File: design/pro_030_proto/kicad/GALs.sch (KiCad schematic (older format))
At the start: 17 parts, among them IC10 ATF22V10C, IC2 ATF22V10C, IC3 ATF22V10C, IC4 ATF22V10C, IC5 ATF22V10C, IC6 ATF22V10C, IC7 ATF22V10C

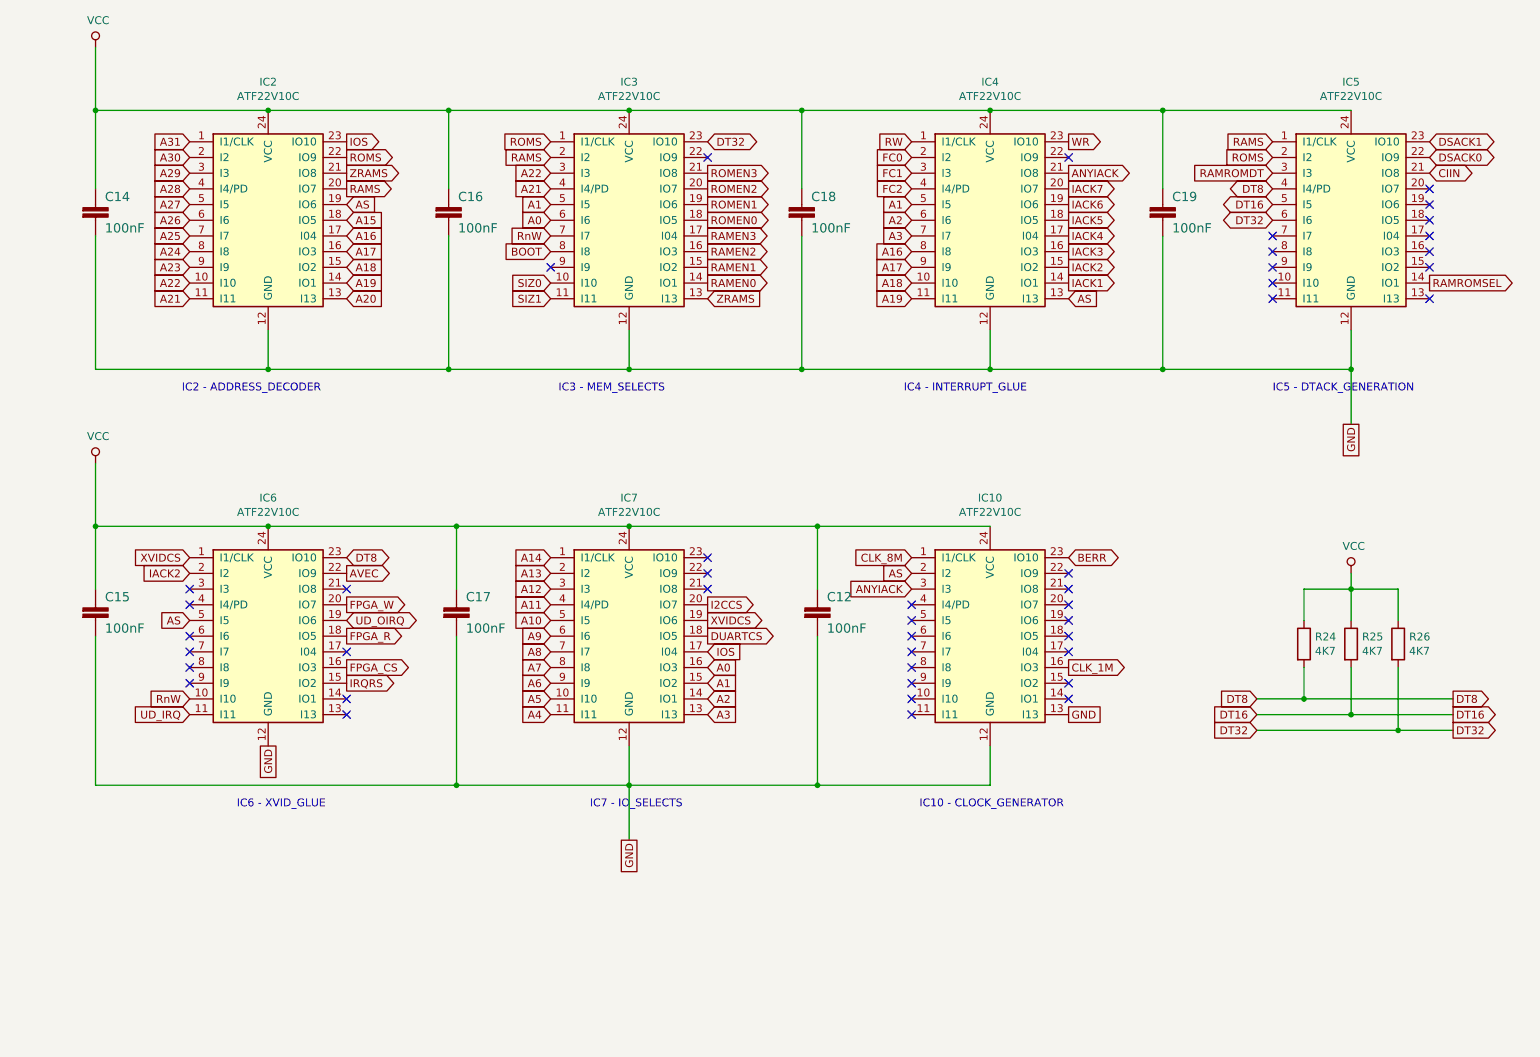
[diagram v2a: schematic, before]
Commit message: Add IC14 GAL into schematic
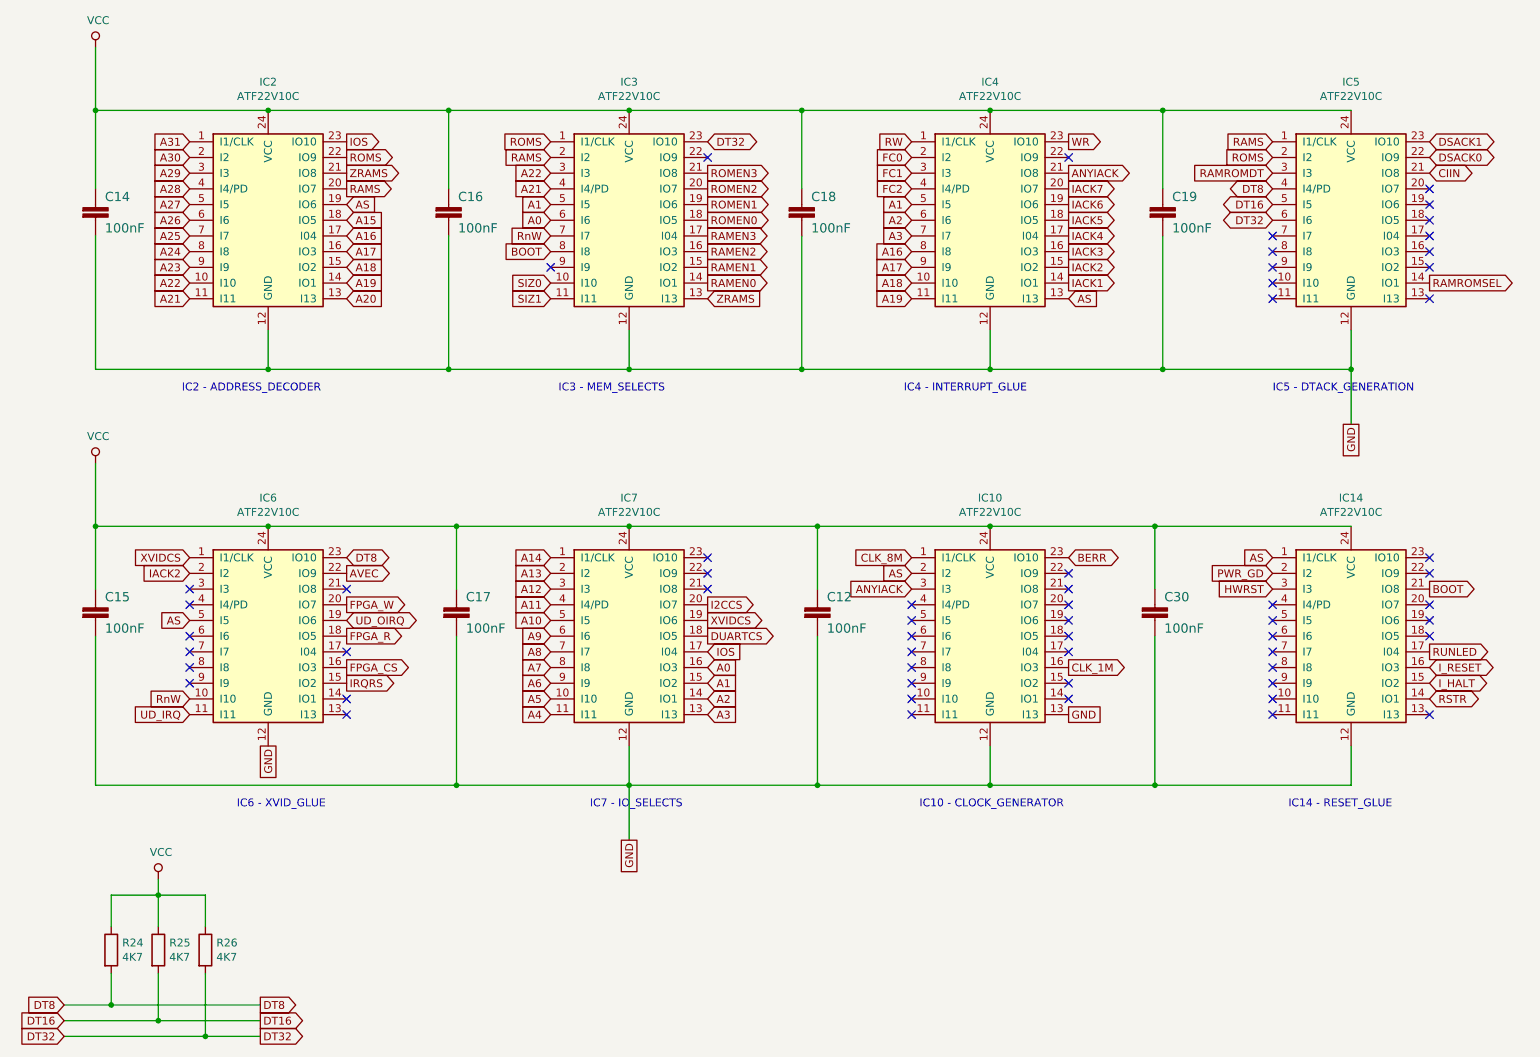
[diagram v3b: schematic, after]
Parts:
- added C30: 100nF, Capacitor_THT:C_Rect_L4.0mm_W2.5mm_P2.50mm, symbol rosco_m68k-eagle-import:C2,5-3
- added IC14: ATF22V10C, Package_DIP:DIP-24_W7.62mm_Socket_LongPads, symbol rosco_m68k:GAL22V10
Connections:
- net AS: now also IC14.1 (I1/CLK)
- net BOOT: now also IC14.21 (IO8)
- net GND: now also C30.2, IC14.12 (GND)
- net VCC: now also C30.1, IC14.24 (VCC)
- new net HWRST: IC14.3 (I3)
- new net I_HALT: IC14.15 (IO2)
- new net I_RESET: IC14.16 (IO3)
- new net PWR_GD: IC14.2 (I2)
- new net RSTR: IC14.14 (IO1)
- new net RUNLED: IC14.17 (I04)
- no-connect marks 44 -> 58
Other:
- note added: "IC14 - RESET_GLUE"
- moved on the sheet: R24, R25, R26
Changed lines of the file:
@@
 NoConn ~ 8800 2650
 NoConn ~ 8800 2750
-Text GLabel 8700 5300 0    50   Input ~ 0
+Text GLabel 1100 7250 0    50   Input ~ 0
 DT8
-Text GLabel 8700 5400 0    50   Input ~ 0
+Text GLabel 1100 7350 0    50   Input ~ 0
 DT16
-Text GLabel 8700 5500 0    50   Input ~ 0
+Text GLabel 1100 7450 0    50   Input ~ 0
 DT32
-Text GLabel 9950 5300 2    50   Output ~ 0
+Text GLabel 2350 7250 2    50   Output ~ 0
 DT8
-Text GLabel 9950 5400 2    50   Output ~ 0
+Text GLabel 2350 7350 2    50   Output ~ 0
 DT16
-Text GLabel 9950 5500 2    50   Output ~ 0
+Text GLabel 2350 7450 2    50   Output ~ 0
 DT32
 $Comp
 L Device:R R24
 U 1 1 60FCD0F0
-P 9000 4950
-F 0 "R24" H 9070 4996 50  0000 L CNN
-F 1 "4K7" H 9070 4905 50  0000 L CNN
-F 2 "rosco_m68k:R-0207_10" V 8930 4950 50  0001 C CNN
-F 3 "~" H 9000 4950 50  0001 C CNN
-	1    9000 4950
+P 1400 6900
+F 0 "R24" H 1470 6946 50  0000 L CNN
+F 1 "4K7" H 1470 6855 50  0000 L CNN
+F 2 "rosco_m68k:R-0207_10" V 1330 6900 50  0001 C CNN
+F 3 "~" H 1400 6900 50  0001 C CNN
+	1    1400 6900
 	1    0    0    -1
 $EndComp
@@
 L Device:R R25
 U 1 1 60FCDD0E
-P 9300 4950
-F 0 "R25" H 9370 4996 50  0000 L CNN
-F 1 "4K7" H 9370 4905 50  0000 L CNN
-F 2 "rosco_m68k:R-0207_10" V 9230 4950 50  0001 C CNN
-F 3 "~" H 9300 4950 50  0001 C CNN
-	1    9300 4950
+P 1700 6900
+F 0 "R25" H 1770 6946 50  0000 L CNN
+F 1 "4K7" H 1770 6855 50  0000 L CNN
+F 2 "rosco_m68k:R-0207_10" V 1630 6900 50  0001 C CNN
+F 3 "~" H 1700 6900 50  0001 C CNN
+	1    1700 6900
 	1    0    0    -1
 $EndComp
@@
 L Device:R R26
 U 1 1 60FCE353
-P 9600 4950
-F 0 "R26" H 9670 4996 50  0000 L CNN
-F 1 "4K7" H 9670 4905 50  0000 L CNN
-F 2 "rosco_m68k:R-0207_10" V 9530 4950 50  0001 C CNN
-F 3 "~" H 9600 4950 50  0001 C CNN
-	1    9600 4950
+P 2000 6900
+F 0 "R26" H 2070 6946 50  0000 L CNN
+F 1 "4K7" H 2070 6855 50  0000 L CNN
+F 2 "rosco_m68k:R-0207_10" V 1930 6900 50  0001 C CNN
+F 3 "~" H 2000 6900 50  0001 C CNN
+	1    2000 6900
 	1    0    0    -1
 $EndComp
@@
 L power:VCC #PWR033
 U 1 1 60FCF006
-P 9300 4500
-F 0 "#PWR033" H 9300 4350 50  0001 C CNN
-F 1 "VCC" H 9317 4673 50  0000 C CNN
-F 2 "" H 9300 4500 50  0001 C CNN
-F 3 "" H 9300 4500 50  0001 C CNN
-	1    9300 4500
-	1    0    0    -1
-$EndComp
-Wire Wire Line
-	9000 4800 9000 4600
-Wire Wire Line
-	9000 4600 9300 4600
-Wire Wire Line
-	9300 4600 9300 4500
-Wire Wire Line
-	9300 4600 9600 4600
-Wire Wire Line
-	9600 4600 9600 4800
-Connection ~ 9300 4600
-Wire Wire Line
-	8700 5300 9000 5300
-Wire Wire Line
-	8700 5400 9300 5400
-Wire Wire Line
-	8700 5500 9600 5500
-Wire Wire Line
-	9000 5100 9000 5300
-Connection ~ 9000 5300
-Wire Wire Line
-	9000 5300 9950 5300
-Wire Wire Line
-	9300 5100 9300 5400
-Connection ~ 9300 5400
-Wire Wire Line
-	9300 5400 9950 5400
-Wire Wire Line
-	9600 5100 9600 5500
-Connection ~ 9600 5500
-Wire Wire Line
-	9600 5500 9950 5500
+P 1700 6450
+F 0 "#PWR033" H 1700 6300 50  0001 C CNN
+F 1 "VCC" H 1717 6623 50  0000 C CNN
+F 2 "" H 1700 6450 50  0001 C CNN
+F 3 "" H 1700 6450 50  0001 C CNN
+	1    1700 6450
+	1    0    0    -1
+$EndComp
+Wire Wire Line
+	1400 6750 1400 6550
+Wire Wire Line
+	1400 6550 1700 6550
+Wire Wire Line
+	1700 6550 1700 6450
+Wire Wire Line
+	1700 6550 2000 6550
+Wire Wire Line
+	2000 6550 2000 6750
+Connection ~ 1700 6550
+Wire Wire Line
+	1100 7250 1400 7250
+Wire Wire Line
+	1100 7350 1700 7350
+Wire Wire Line
+	1100 7450 2000 7450
+Wire Wire Line
+	1400 7050 1400 7250
+Connection ~ 1400 7250
+Wire Wire Line
+	1400 7250 2350 7250
+Wire Wire Line
+	1700 7050 1700 7350
+Connection ~ 1700 7350
+Wire Wire Line
+	1700 7350 2350 7350
+Wire Wire Line
+	2000 7050 2000 7450
+Connection ~ 2000 7450
+Wire Wire Line
+	2000 7450 2350 7450
 Text GLabel 8800 1750 0    50   Input ~ 0
 RAMS
@@
 BOOT
 Wire Wire Line
-	9300 4600 9300 4800
+	1700 6550 1700 6750
 Wire Wire Line
 	2400 4200 3600 4200
@@
 NoConn ~ 7500 4800
 NoConn ~ 7500 4700
+$Comp
+L rosco_m68k:GAL22V10 IC?
+U 1 1 616B7896
+P 9300 4900
+AR Path="/61161E57/616B7896" Ref="IC?"  Part="1"
+AR Path="/6103896C/616B7896" Ref="IC14"  Part="1"
+F 0 "IC14" H 9300 5781 50  0000 C CNN
+F 1 "ATF22V10C" H 9300 5690 50  0000 C CNN
+F 2 "Package_DIP:DIP-24_W7.62mm_Socket_LongPads" H 9300 4900 50  0001 C CNN
+F 3 "https://www.mouser.com/datasheet/2/268/doc0735-1369018.pdf" H 9300 4900 50  0001 C CNN
+	1    9300 4900
+	1    0    0    -1
+$EndComp
+Text GLabel 8800 4400 0    50   Input ~ 0
+AS
+Text GLabel 8800 4500 0    50   Input ~ 0
+PWR_GD
+Text GLabel 8800 4600 0    50   Input ~ 0
+HWRST
+NoConn ~ 9800 4500
+NoConn ~ 8800 4700
+NoConn ~ 8800 4800
+NoConn ~ 8800 4900
+NoConn ~ 8800 5000
+NoConn ~ 8800 5100
+NoConn ~ 8800 5200
+NoConn ~ 8800 5300
+NoConn ~ 8800 5400
+NoConn ~ 9800 4900
+NoConn ~ 9800 4800
+NoConn ~ 9800 4700
+$Comp
+L rosco_m68k-eagle-import:C2,5-3 C?
+U 1 1 616BA5ED
+P 8050 4700
+AR Path="/616BA5ED" Ref="C?"  Part="1"
+AR Path="/5E53B810/616BA5ED" Ref="C?"  Part="1"
+AR Path="/5E53B952/616BA5ED" Ref="C?"  Part="1"
+AR Path="/6103896C/616BA5ED" Ref="C30"  Part="1"
+F 0 "C30" H 8110 4715 59  0000 L BNN
+F 1 "100nF" H 8110 4515 59  0000 L BNN
+F 2 "Capacitor_THT:C_Rect_L4.0mm_W2.5mm_P2.50mm" H 8050 4700 50  0001 C CNN
+F 3 "" H 8050 4700 50  0001 C CNN
+	1    8050 4700
+	1    0    0    -1
+$EndComp
+Wire Wire Line
+	8050 4900 8050 5850
+Wire Wire Line
+	8050 4200 8050 4600
+Wire Wire Line
+	7000 4200 8050 4200
+Connection ~ 7000 4200
+Wire Wire Line
+	8050 4200 9300 4200
+Connection ~ 8050 4200
+Wire Wire Line
+	7000 5850 8050 5850
+Connection ~ 7000 5850
+Wire Wire Line
+	9300 5600 9300 5850
+Wire Wire Line
+	9300 5850 8050 5850
+Connection ~ 8050 5850
+NoConn ~ 9800 5400
+NoConn ~ 9800 4400
+Text GLabel 9800 5300 2    50   3State ~ 0
+RSTR
+Text GLabel 9800 5200 2    50   3State ~ 0
+I_HALT
+Text GLabel 9800 5100 2    50   3State ~ 0
+I_RESET
+Text GLabel 9800 5000 2    50   Output ~ 0
+RUNLED
+Text GLabel 9800 4600 2    50   Output ~ 0
+BOOT
+Text Notes 8900 6000 0    50   ~ 0
+IC14 - RESET_GLUE
 $EndSCHEMATC
